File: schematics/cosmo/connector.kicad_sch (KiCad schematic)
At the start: 5 parts

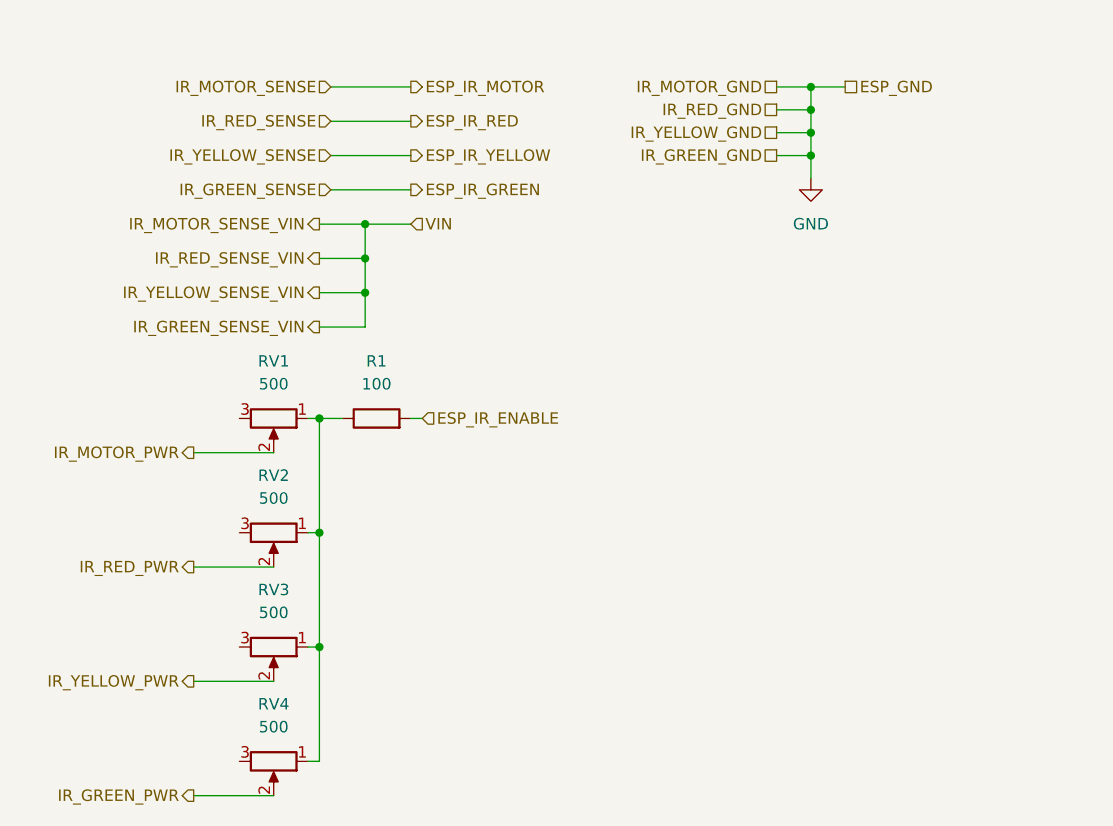
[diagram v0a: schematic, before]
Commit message: Add PD resistors to sense pins, integrate connector into main schematic
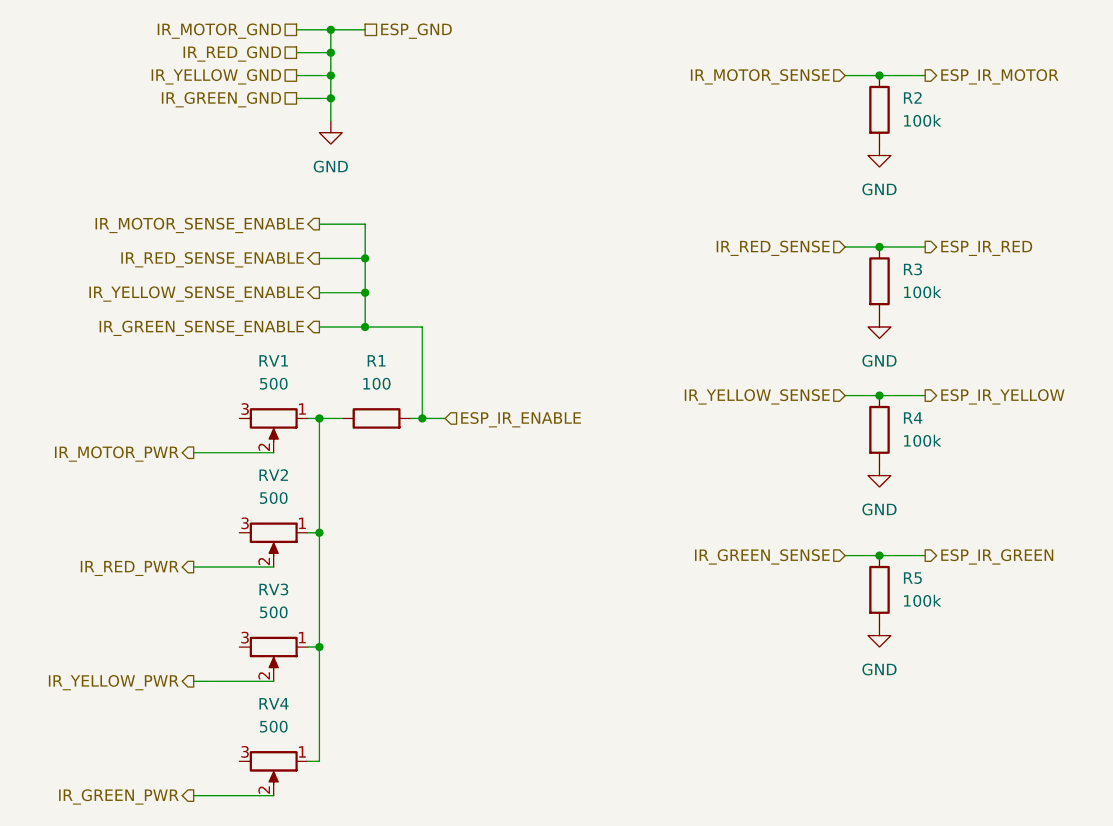
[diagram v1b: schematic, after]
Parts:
- added R2, R3, R4, R5: 100k, symbol Device:R
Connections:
- net ESP_IR_GREEN: now also R5.1
- net ESP_IR_MOTOR: now also R2.1
- net ESP_IR_RED: now also R3.1
- net ESP_IR_YELLOW: now also R4.1
- net GND: now also R2.2, R3.2, R4.2, R5.2

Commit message: Select connector footprints (WIP)
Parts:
- R1, R2, R3, R4, R5: footprint (none) -> Resistor_THT:R_Axial_DIN0207_L6.3mm_D2.5mm_P7.62mm_Horizontal
- RV1, RV2, RV3, RV4: footprint (none) -> Potentiometer_THT:Potentiometer_Bourns_3296W_Vertical
